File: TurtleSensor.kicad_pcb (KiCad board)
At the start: 2 copper layers, 72 x 72 mm, 13 parts, among them IC1 ATMEGA328-P, J1 ISPConnector, J2 FTDIConnector, U1 HTU21DBreakout, U2 W25Q32FlashBreakout

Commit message: added copyright
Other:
- board text added: "© Erik Meike 2016"
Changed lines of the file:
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@@
     (area 95.949999 85.949999 168.050001 158.050001)
     (thickness 1.6)
-    (drawings 4)
+    (drawings 6)
     (tracks 139)
     (zones 0)
@@
     )
   )
+  (gr_text "© Erik Meike 2016" (at 132 152) (layer F.SilkS)
+    (effects (font (size 1.5 1.5) (thickness 0.3)))
+  )
+  (gr_text "© Erik Meike 2016" (at 132 152) (layer F.Cu)
+    (effects (font (size 1.5 1.5) (thickness 0.3)))
+  )
   (gr_line (start 168 158) (end 96 158) (angle 90) (layer Edge.Cuts) (width 0.1))

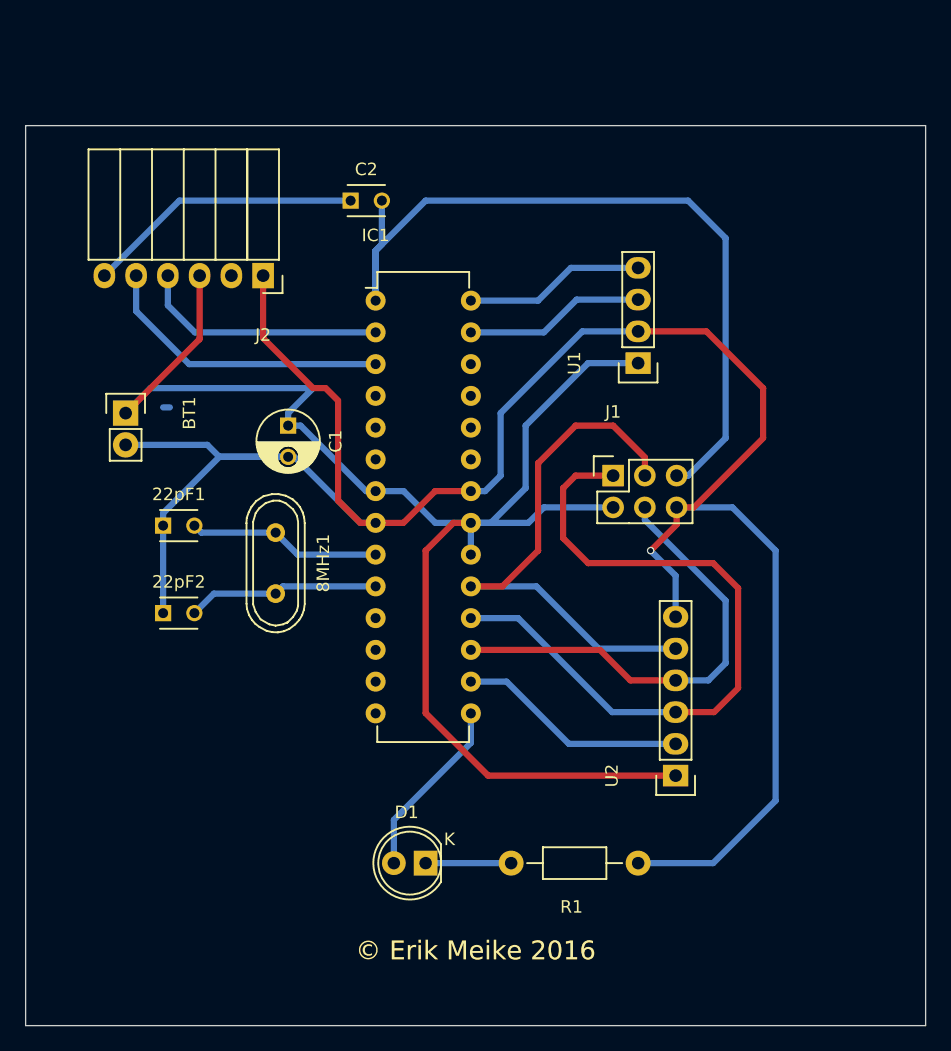
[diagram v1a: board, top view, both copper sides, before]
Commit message: mostly routed
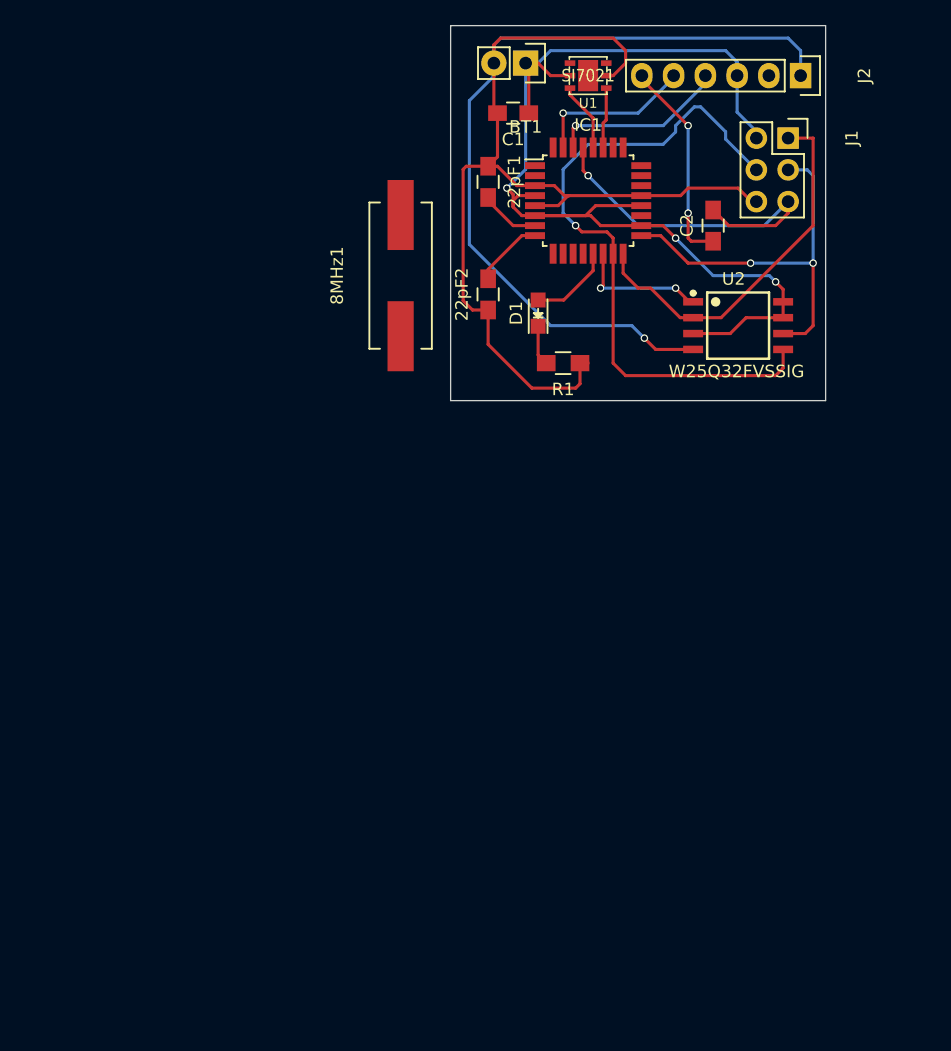
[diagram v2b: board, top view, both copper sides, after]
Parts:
- 22pF1, 22pF2, C2: footprint Capacitors_ThroughHole:C_Disc_D3_P2.5 -> Capacitors_SMD:C_0805_HandSoldering
- 8MHz1: footprint Crystals:Crystal_HC49-U_Vertical -> Crystals:Crystal_HC49-SD_SMD
- C1: value 25µF -> 10µF; footprint Capacitors_ThroughHole:C_Radial_D5_L11_P2.5 -> Capacitors_SMD:C_0805_HandSoldering
- D1: footprint LEDs:LED-5MM -> LEDs:LED_0805
- IC1: value ATMEGA328-P -> ATMEGA328P-A; footprint Housings_DIP:DIP-28_W7.62mm -> Housings_QFP:TQFP-32_7x7mm_Pitch0.8mm
- J2: footprint Socket_Strips:Socket_Strip_Angled_1x06 -> Pin_Headers:Pin_Header_Straight_1x06
- R1: footprint Resistors_ThroughHole:Resistor_Horizontal_RM10mm -> Resistors_SMD:R_0805_HandSoldering
- U1: value HTU21DBreakout -> SI7021; footprint Socket_Strips:Socket_Strip_Straight_1x04 -> SI7021:DFN-6%2f3MM
- U2: value W25Q32FlashBreakout -> W25Q32FVSSIG; footprint Socket_Strips:Socket_Strip_Straight_1x06 -> W25Q32FVSSIG:SOIC127P790X216-8N
- moved J2 45.9 mm to (158.0, 82.0), turned to 270 degrees
- moved D1 44.9 mm to (137.0, 101.0), turned to 90 degrees
- moved BT1 42.5 mm to (136.0, 81.0), turned to 180 degrees
- moved R1 40.4 mm to (139.0, 105.0)
- moved 22pF1 37.8 mm to (133.0, 90.5), turned to 270 degrees
- moved 22pF2 36.4 mm to (133.0, 99.5), turned to 90 degrees
- moved U2 36.3 mm to (153.0, 102.0), turned to 0 degrees
- moved C1 30.8 mm to (135.0, 85.0), turned to 180 degrees
- moved J1 30.4 mm to (157.0, 87.0), turned to 270 degrees
- moved C2 29.1 mm to (151.0, 94.0), turned to 90 degrees
- moved 8MHz1 25.1 mm to (126.0, 98.0), turned to 90 degrees
- moved U1 23.3 mm to (141.0, 82.0), turned to 180 degrees
- moved IC1 18.8 mm to (141.0, 92.0)
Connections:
- IC1 pad 1: /~RST -> Net-(IC1-Pad1)
- IC1 pad 10: Net-(22pF2-Pad2) -> Net-(IC1-Pad10)
- IC1 pad 13: Net-(IC1-Pad13) -> Net-(D1-Pad2)
- IC1 pad 14: Net-(IC1-Pad14) -> /~CS
- IC1 pad 15: Net-(D1-Pad2) -> /MOSI
- IC1 pad 16: /~CS -> /MISO
- IC1 pad 17: /MOSI -> /SCK
- IC1 pad 18: /MISO -> +BATT
- IC1 pad 19: /SCK -> Net-(IC1-Pad19)
- IC1 pad 2: /RX -> Net-(IC1-Pad2)
- IC1 pad 21: +BATT -> GND
- IC1 pad 22: GND -> Net-(IC1-Pad22)
- IC1 pad 3: /TX -> GND
- IC1 pad 4: Net-(IC1-Pad4) -> +BATT
- IC1 pad 5: Net-(IC1-Pad5) -> GND
- IC1 pad 6: Net-(IC1-Pad6) -> +BATT
- IC1 pad 7: +BATT -> Net-(22pF1-Pad2)
- IC1 pad 8: GND -> Net-(22pF2-Pad2)
- IC1 pad 9: Net-(22pF1-Pad2) -> Net-(IC1-Pad9)
- U1 pad 1: +BATT -> /SDA
- U1 pad 3: /SDA -> (no net)
- U1 pad 4: /SCL -> (no net)
- U2 pad 1: +BATT -> /~CS
- U2 pad 2: /~CS -> /MISO
- U2 pad 3: /MISO -> +BATT
- U2 pad 4: /MOSI -> GND
- U2 pad 5: /SCK -> /MOSI
- U2 pad 6: GND -> /SCK
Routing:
- net /~RST: track 68.3 -> 28.7 mm, vias 0 -> 1
- net GND: track 181.0 -> 144.7 mm
- net +BATT: track 126.6 -> 90.4 mm, vias 0 -> 3
- net /MISO: track 57.4 -> 30.3 mm
- net /MOSI: track 37.1 -> 54.3 mm, vias 0 -> 1
- net /SCK: track 44.3 -> 31.5 mm, vias 0 -> 2
- net Net-(22pF1-Pad2): track 15.5 -> 4.83 mm
- net /TX: track 23.8 -> 13.7 mm, vias 0 -> 1
- net Net-(22pF2-Pad2): track 15.4 -> 5.62 mm
- net /SDA: track 14.5 -> 4.85 mm
- net /SCL: track 14.5 -> 5.73 mm
- net Net-(D1-Pad2): track 14.5 -> 6.72 mm
- net /~CS: track 18.4 -> 10.7 mm, vias 0 -> 2
- net /RX: track 20.3 -> 14.2 mm, vias 0 -> 1
- net Net-(C2-Pad1): track 22.2 -> 17.3 mm, vias 0 -> 2
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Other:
- board size 72 x 72 mm -> 30 x 30 mm
- net class Default: trace_width 0.5 -> 0.25
- board text removed: "© Erik Meike 2016"

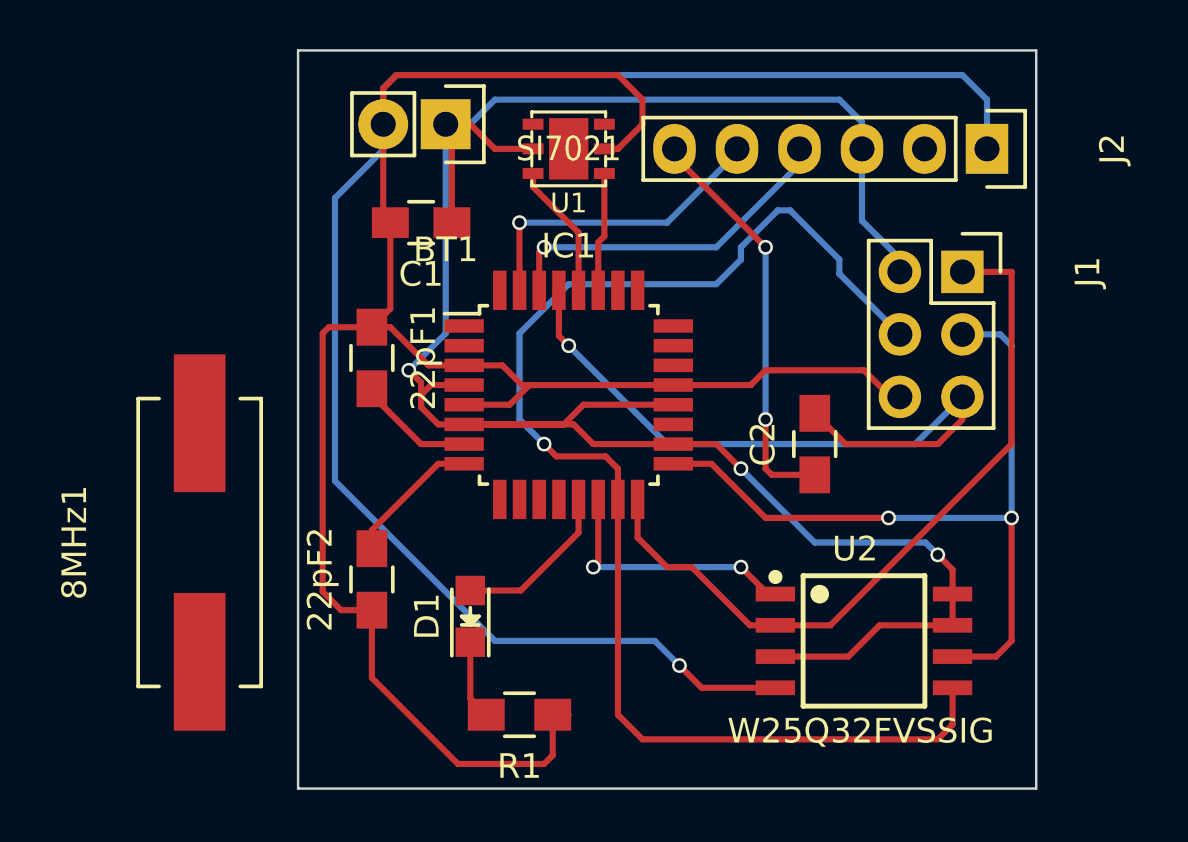
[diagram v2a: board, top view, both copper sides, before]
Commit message: added missing pullups and lots
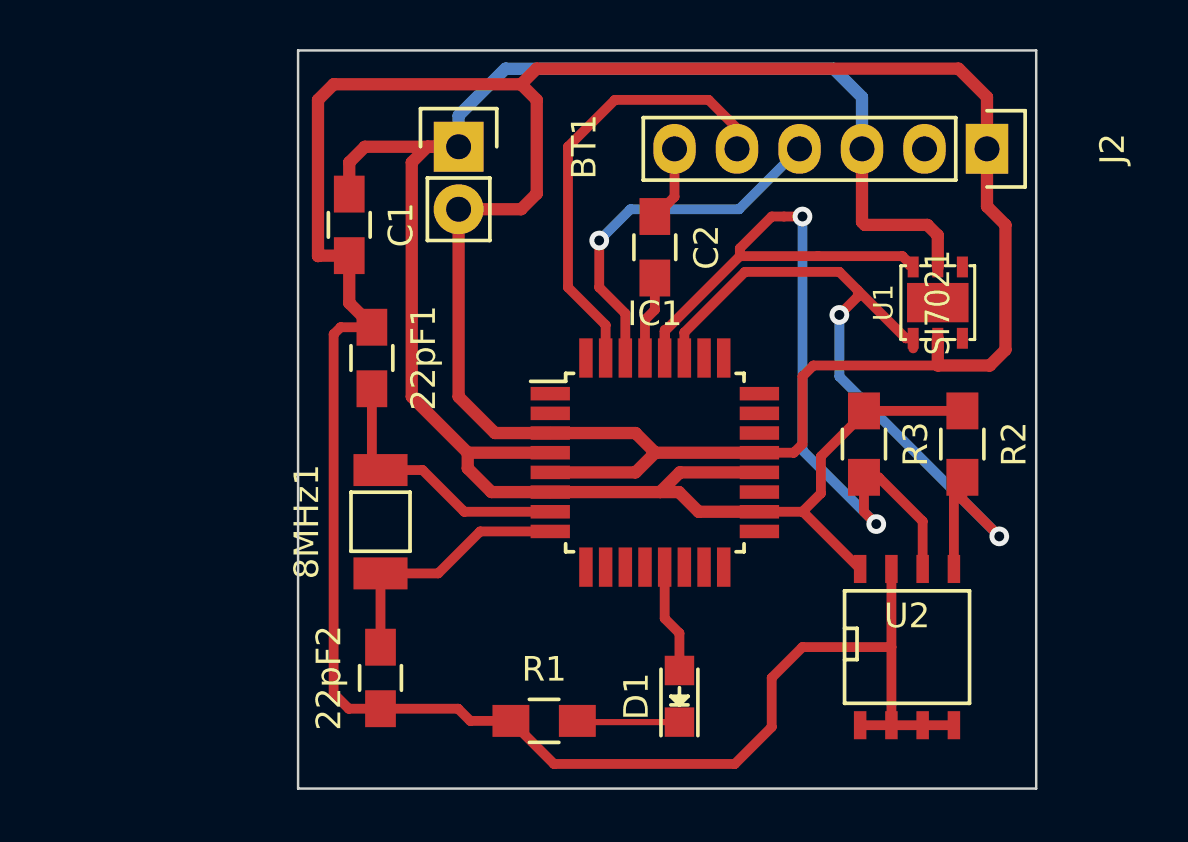
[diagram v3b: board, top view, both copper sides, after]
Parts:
- removed J1: ISPConnector, Socket_Strips:Socket_Strip_Straight_2x03
- added R2: 4k, Resistors_SMD:R_0805_HandSoldering, F.Cu at (157.0, 94.0)
- added R3: 4k, Resistors_SMD:R_0805_HandSoldering, F.Cu at (153.0, 94.0)
- 8MHz1: footprint Crystals:Crystal_HC49-SD_SMD -> footprints:2-SMD
- U2: value W25Q32FVSSIG -> M24512; footprint W25Q32FVSSIG:SOIC127P790X216-8N -> SMD_Packages:SOIC-8-N
- moved U1 16.2 mm to (156.0, 88.2), turned to 90 degrees
- moved C2 10.3 mm to (144.5, 86.0), turned to 270 degrees
- moved D1 9.10 mm to (145.5, 104.2)
- moved 8MHz1 7.40 mm to (133.3, 97.2), turned to 270 degrees
- moved IC1 4.45 mm to (144.5, 94.8)
- moved 22pF2 4.02 mm to (133.3, 103.5)
- moved C1 2.92 mm to (132.1, 85.1), turned to 270 degrees
- moved U2 1.77 mm to (154.8, 102.2)
- moved BT1 1.05 mm to (136.5, 81.9), turned to 270 degrees
- moved R1 1.03 mm to (140.0, 105.2), turned to 0 degrees
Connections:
- IC1 pad 1: Net-(IC1-Pad1) -> (no net)
- IC1 pad 10: Net-(IC1-Pad10) -> (no net)
- IC1 pad 11: Net-(IC1-Pad11) -> (no net)
- IC1 pad 12: Net-(IC1-Pad12) -> (no net)
- IC1 pad 14: /~CS -> (no net)
- IC1 pad 15: /MOSI -> (no net)
- IC1 pad 16: /MISO -> (no net)
- IC1 pad 17: /SCK -> (no net)
- IC1 pad 19: Net-(IC1-Pad19) -> (no net)
- IC1 pad 2: Net-(IC1-Pad2) -> (no net)
- IC1 pad 22: Net-(IC1-Pad22) -> (no net)
- IC1 pad 23: Net-(IC1-Pad23) -> (no net)
- IC1 pad 24: Net-(IC1-Pad24) -> (no net)
- IC1 pad 25: Net-(IC1-Pad25) -> (no net)
- IC1 pad 26: Net-(IC1-Pad26) -> (no net)
- IC1 pad 32: Net-(IC1-Pad32) -> (no net)
- IC1 pad 9: Net-(IC1-Pad9) -> (no net)
- J2 pad 2: Net-(J2-Pad2) -> (no net)
- U2 pad 1: /~CS -> GND
- U2 pad 2: /MISO -> GND
- U2 pad 3: +BATT -> GND
- U2 pad 5: /MOSI -> /SDA
- U2 pad 6: /SCK -> /SCL
- U2 pad 7: +BATT -> GND
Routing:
- net /MOSI: track 54.3 -> 0.00 mm, vias 1 -> 0
- net /SCL: track 5.73 -> 39.4 mm, vias 0 -> 2
- net /SCK: track 31.5 -> 0.00 mm, vias 2 -> 0
- net /MISO: track 30.3 -> 0.00 mm
- net /SDA: track 4.85 -> 32.8 mm, vias 0 -> 2
- net /~RST: track 28.7 -> 3.42 mm, vias 1 -> 0
- net Net-(C2-Pad1): track 17.3 -> 3.38 mm, vias 2 -> 0
- net /~CS: track 10.7 -> 0.00 mm, vias 2 -> 0
- net GND: track 144.7 -> 151.8 mm, vias 1 -> 0
- net Net-(22pF1-Pad2): track 4.83 -> 11.8 mm
- net /TX: track 13.7 -> 20.0 mm, vias 1 -> 0
- net +BATT: track 90.4 -> 84.6 mm, vias 3 -> 0
- net Net-(22pF2-Pad2): track 5.62 -> 10.6 mm
- net Net-(D1-Pad2): track 6.72 -> 4.45 mm
- net /RX: track 14.2 -> 16.2 mm
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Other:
- net class Default: trace_width 0.25 -> 0.4; via_dia 0.6 -> 0.8
- net class Power added: clearance 0.2, trace_width 0.5, via_dia 1, via_drill 0.4
- rule trace_min: 0.2 -> 0.3
- rule via_min_drill: 0.3 -> 0.34
- rule via_min_size: 0.4 -> 0.7
